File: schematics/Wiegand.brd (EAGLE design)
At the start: 78.7 x 58.4 mm, 67 parts, among them J1 AVR_SPI_PRG_6NS, Q1 NTR1P02T1G, Q2 NTR1P02T1G, U1 ATMEGA168, U2 RS485_SP491, U4 MOC3063, U5 MOC3063, U6 MOC3063, U7 MOC3063, U8 MOC3063, U9 MOC3063, Y1 16Mhz

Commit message: minor changes to board, adding firmware and eagleup render
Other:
- board text added: "Rev B - 2014-01-05"
- board text removed: "Rev B - 2014-01-01"
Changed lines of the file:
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@@
 <setting verticaltext="up"/>
 </settings>
-<grid distance="10" unitdist="mil" unit="mil" style="lines" multiple="1" display="no" altdistance="1" altunitdist="mil" altunit="mil"/>
+<grid distance="10" unitdist="mil" unit="mil" style="lines" multiple="1" display="no" altdistance="5" altunitdist="mil" altunit="mil"/>
 <layers>
 <layer number="1" name="Top" color="4" fill="1" visible="yes" active="yes"/>
 <layer number="2" name="Route2" color="13" fill="3" visible="no" active="yes"/>
 <layer number="15" name="Route15" color="17" fill="6" visible="no" active="yes"/>
-<layer number="16" name="Bottom" color="1" fill="1" visible="yes" active="yes"/>
+<layer number="16" name="Bottom" color="1" fill="1" visible="no" active="yes"/>
 <layer number="17" name="Pads" color="2" fill="1" visible="yes" active="yes"/>
 <layer number="18" name="Vias" color="2" fill="1" visible="yes" active="yes"/>
@@
 <layer number="20" name="Dimension" color="18" fill="1" visible="yes" active="yes"/>
 <layer number="21" name="tPlace" color="7" fill="1" visible="yes" active="yes"/>
-<layer number="22" name="bPlace" color="3" fill="1" visible="yes" active="yes"/>
+<layer number="22" name="bPlace" color="3" fill="1" visible="no" active="yes"/>
 <layer number="23" name="tOrigins" color="15" fill="1" visible="yes" active="yes"/>
-<layer number="24" name="bOrigins" color="3" fill="1" visible="yes" active="yes"/>
+<layer number="24" name="bOrigins" color="3" fill="1" visible="no" active="yes"/>
 <layer number="25" name="tNames" color="7" fill="1" visible="yes" active="yes"/>
-<layer number="26" name="bNames" color="3" fill="1" visible="yes" active="yes"/>
+<layer number="26" name="bNames" color="3" fill="1" visible="no" active="yes"/>
 <layer number="27" name="tValues" color="7" fill="1" visible="no" active="yes"/>
 <layer number="28" name="bValues" color="3" fill="1" visible="no" active="yes"/>
-<layer number="29" name="tStop" color="7" fill="3" visible="no" active="yes"/>
+<layer number="29" name="tStop" color="7" fill="3" visible="yes" active="yes"/>
 <layer number="30" name="bStop" color="7" fill="6" visible="no" active="yes"/>
-<layer number="31" name="tCream" color="7" fill="4" visible="no" active="yes"/>
+<layer number="31" name="tCream" color="7" fill="4" visible="yes" active="yes"/>
 <layer number="32" name="bCream" color="7" fill="5" visible="no" active="yes"/>
 <layer number="33" name="tFinish" color="6" fill="3" visible="no" active="yes"/>
@@
 <layer number="35" name="tGlue" color="7" fill="4" visible="no" active="yes"/>
 <layer number="36" name="bGlue" color="7" fill="5" visible="no" active="yes"/>
-<layer number="37" name="tTest" color="7" fill="1" visible="yes" active="yes"/>
-<layer number="38" name="bTest" color="7" fill="1" visible="yes" active="yes"/>
-<layer number="39" name="tKeepout" color="4" fill="11" visible="no" active="yes"/>
-<layer number="40" name="bKeepout" color="1" fill="11" visible="no" active="yes"/>
-<layer number="41" name="tRestrict" color="4" fill="10" visible="no" active="yes"/>
+<layer number="37" name="tTest" color="7" fill="1" visible="no" active="yes"/>
+<layer number="38" name="bTest" color="7" fill="1" visible="no" active="yes"/>
+<layer number="39" name="tKeepout" color="4" fill="11" visible="yes" active="yes"/>
+<layer number="40" name="bKeepout" color="1" fill="11" visible="yes" active="yes"/>
+<layer number="41" name="tRestrict" color="4" fill="10" visible="yes" active="yes"/>
 <layer number="42" name="bRestrict" color="1" fill="10" visible="no" active="yes"/>
 <layer number="43" name="vRestrict" color="2" fill="10" visible="no" active="yes"/>
@@
 <layer number="45" name="Holes" color="7" fill="1" visible="yes" active="yes"/>
 <layer number="46" name="Milling" color="3" fill="1" visible="yes" active="yes"/>
-<layer number="47" name="Measures" color="7" fill="1" visible="no" active="yes"/>
+<layer number="47" name="Measures" color="7" fill="1" visible="yes" active="yes"/>
 <layer number="48" name="Document" color="7" fill="1" visible="no" active="yes"/>
 <layer number="49" name="Reference" color="7" fill="1" visible="no" active="yes"/>
 <layer number="50" name="dxf" color="7" fill="1" visible="no" active="yes"/>
-<layer number="51" name="tDocu" color="7" fill="2" visible="no" active="yes"/>
+<layer number="51" name="tDocu" color="7" fill="2" visible="yes" active="yes"/>
 <layer number="52" name="bDocu" color="3" fill="2" visible="no" active="yes"/>
 <layer number="91" name="Nets" color="2" fill="1" visible="no" active="no"/>
@@
 <text x="52.578" y="54.61" size="2.1844" layer="25" font="vector" ratio="16">MakerPass</text>
 <text x="52.324" y="51.816" size="1.6764" layer="25" font="vector" ratio="16">Wiegand Board</text>
-<text x="54.356" y="1.016" size="1.016" layer="25" font="vector" ratio="16">Rev B - 2014-01-01</text>
+<text x="54.356" y="1.016" size="1.016" layer="25" font="vector" ratio="16">Rev B - 2014-01-05</text>
 <text x="68.072" y="46.99" size="3.81" layer="26" font="vector" ratio="16" rot="MR0">MakerPass</text>
 <wire x1="65.786" y1="14.478" x2="65.786" y2="10.414" width="0.254" layer="25" style="shortdash"/>
@@
 <text x="25.146" y="33.274" size="1.27" layer="21" ratio="16" rot="R270">Status</text>
 <text x="68.072" y="44.45" size="1.778" layer="22" ratio="16" rot="MR0">Wiegand Board</text>
-<text x="78.232" y="39.753" size="1.016" layer="25" ratio="16" rot="R90">12V</text>
+<text x="78.232" y="39.499" size="1.016" layer="25" ratio="16" rot="R90">12V</text>
 <text x="78.232" y="46.555" size="1.016" layer="25" ratio="16" rot="R90">GND</text>
 <text x="78.232" y="19.444" size="1.778" layer="25" ratio="16" rot="R90">A</text>
@@
 <text x="78.232" y="43.253" size="1.016" layer="25" ratio="16" rot="R90">GND</text>
 <text x="78.232" y="36.451" size="1.016" layer="25" ratio="16" rot="R90">5V</text>
-<text x="78.232" y="22.171" size="1.016" layer="25" ratio="16" rot="R90">RXD</text>
-<text x="78.486" y="25.727" size="1.016" layer="25" ratio="16" rot="R90">TXD</text>
-<text x="78.232" y="29.283" size="1.016" layer="25" ratio="16" rot="R90">D0</text>
+<text x="78.232" y="21.917" size="1.016" layer="25" ratio="16" rot="R90">RXD</text>
+<text x="78.232" y="25.473" size="1.016" layer="25" ratio="16" rot="R90">TXD</text>
+<text x="78.232" y="29.537" size="1.016" layer="25" ratio="16" rot="R90">D0</text>
 <text x="78.232" y="33.093" size="1.016" layer="25" ratio="16" rot="R90">D1</text>
 <text x="61.722" y="22.352" size="1.016" layer="26" font="vector" ratio="16" rot="MR0">Design by:
@@
 <element name="Y1" library="SparkFun" package="HC49UP" value="16Mhz" x="13.716" y="31.242" smashed="yes" rot="R180">
 <attribute name="MFG_PN" value="FOXSDLF/160-20" x="13.716" y="31.242" size="1.778" layer="27" rot="R180" display="off"/>
-<attribute name="NAME" x="7.62" y="29.972" size="1.27" layer="25" ratio="16" rot="R180"/>
+<attribute name="NAME" x="7.874" y="34.036" size="1.27" layer="25" ratio="16"/>
 <attribute name="VALUE" x="19.431" y="35.433" size="1.27" layer="27" ratio="10" rot="R180"/>
 </element>
@@
 </signal>
 </signals>
+<errors>
+</errors>
 </board>
 </drawing>

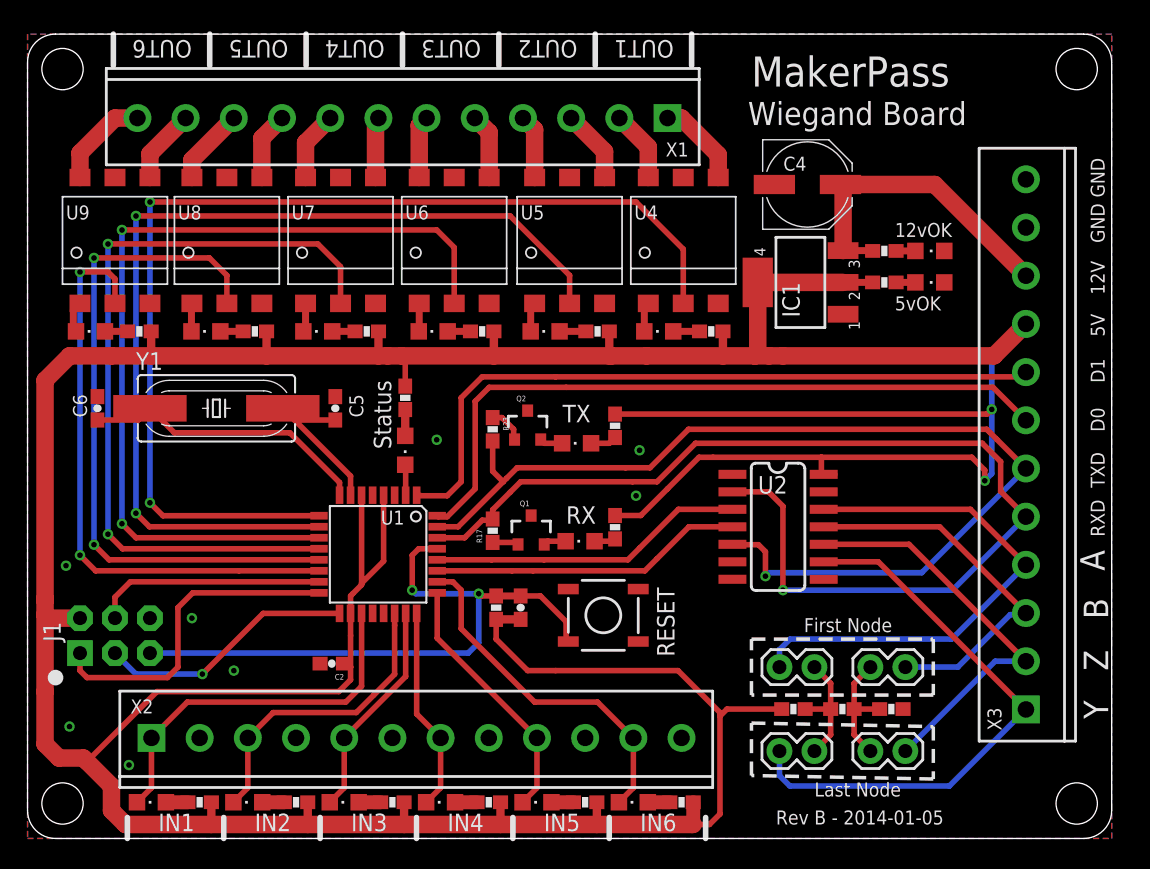
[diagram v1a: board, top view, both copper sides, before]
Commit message: added separate resistors for first / last node, added transistor option atop optoisolators
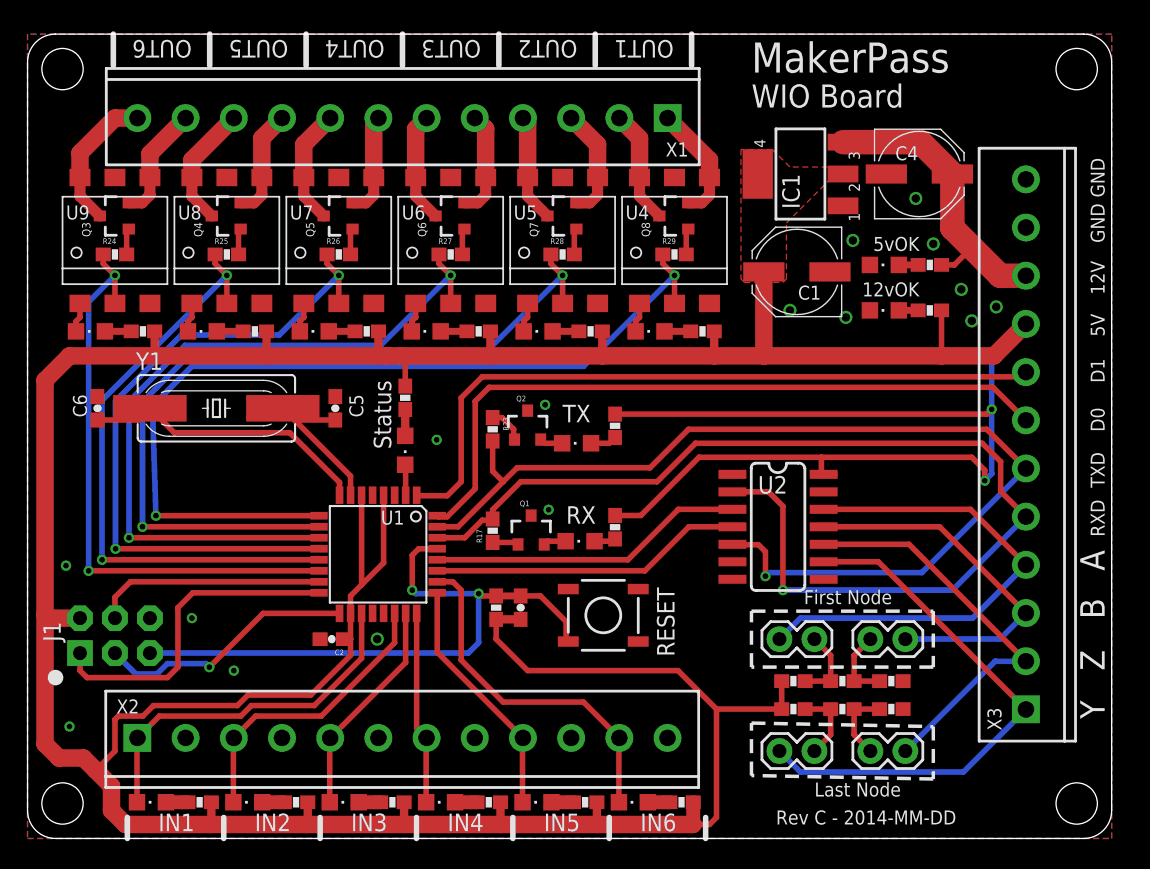
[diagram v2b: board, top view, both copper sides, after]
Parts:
- added C1: 10uF, rcl:PANASONIC_D
- added Q3, Q4, Q5, Q6, Q7, Q8: (no value), LumisenseV6:SOT23-3
- added R24, R25, R26, R27, R28, R29, R31, R32: 1K, SparkFun:0603-RES
- added R30: 100, SparkFun:0603-RES
- C4: value 47uF -> 10uF
- moved LED12 8.76 mm to (37.1, 36.8)
- moved C4 8.16 mm to (64.8, 48.3)
- moved IC1 7.87 mm to (56.1, 48.3)
- moved LED11 7.62 mm to (45.2, 36.8)
- moved LED1 3.88 mm to (62.2, 38.4), turned to 90 degrees
- moved R13 3.88 mm to (65.5, 38.4), turned to 0 degrees
- moved LED4 3.45 mm to (62.2, 41.7), turned to 90 degrees
- moved R18 3.45 mm to (65.5, 41.7), turned to 0 degrees
- moved JP2 2.03 mm to (54.6, 14.5)
- moved JP4 2.03 mm to (63.8, 14.5)
- moved R14 2.03 mm to (55.6, 11.4)
- moved R15 2.03 mm to (59.2, 11.4)
- moved R16 2.03 mm to (62.7, 11.4)
- moved C2 1.78 mm to (22.1, 14.5)
- moved X2 1.02 mm to (7.98, 7.30)
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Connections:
- new net N$43: Q4.1, R25.2
- new net N$435: Q3.1, R24.2
- new net N$44: Q5.1, R26.2
- new net N$48: Q6.1, R27.2
- new net N$49: Q7.1, R28.2
- new net N$50: Q8.1, R29.2
- new net N$51: JP2.2, R14.1, R15.2
- new net N$52: JP4.2, R15.1, R16.2
- net GND: now also C1.-, R32.1
- net N$15: now also LED11.C; no longer LED12.C
- net N$16: now also LED11.A; no longer LED12.A
- net N$17: now also Q8.2
- net N$18: now also Q8.3
- net N$19: now also Q7.2
- net N$20: now also Q7.3
- net N$21: now also LED12.A; no longer LED11.A
- net N$22: now also LED12.C; no longer LED11.C
- net N$23: now also Q6.2
- net N$24: now also Q6.3
- net N$29: now also Q5.2
- net N$3: now also Q4.2
- net N$30: now also Q5.3
- net N$37: now also Q3.3, U9.6, X1.12; no longer U9.4, X1.11
- net N$38: now also Q3.2, U9.4, X1.11; no longer U9.6, X1.12
- net N$4: now also Q4.3
- net N$6: now also R30.1, R32.2; no longer JP4.2, R15.1, R16.2
- net N$7: now also R30.2, R31.1; no longer JP2.2, R14.1, R15.2
- net OUTPUT1: now also R29.1
- net OUTPUT2: now also R28.1
- net OUTPUT3: now also R27.1
- net OUTPUT4: now also R26.1
- net OUTPUT5: now also R25.1
- net OUTPUT6: now also R24.1
- net VCC: now also C1.+, R31.2
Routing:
- net OUTPUT1: track 78.6 -> 65.6 mm
- net OUTPUT2: track 70.6 -> 60.1 mm
- net OUTPUT3: track 64.8 -> 54.8 mm
- net OUTPUT4: track 57.1 -> 49.4 mm
- net OUTPUT5: track 49.8 -> 44.1 mm
- net N$52: track 0.00 -> 5.39 mm
- net N$51: track 0.00 -> 5.39 mm
- net N$37: track 5.39 -> 10.4 mm
- net N$7: track 8.93 -> 5.39 mm
- net N$6: track 8.93 -> 5.39 mm
- net N$24: track 4.54 -> 8.03 mm
- net N$30: track 5.06 -> 8.50 mm
- net N$4: track 5.58 -> 8.97 mm
- net N$20: track 4.67 -> 7.85 mm
- net N$18: track 5.19 -> 8.32 mm
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- added copper zone on layer 1, net VCC
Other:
- board text added: "Rev C - 2014-MM-DD"
- board text added: "WIO Board"
- board text removed: "Rev B - 2014-01-05"
